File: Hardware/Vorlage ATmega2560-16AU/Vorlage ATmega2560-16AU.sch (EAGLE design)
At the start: 152 parts, among them IC1 CD74HC14PW, IC2 ATMEGA2560640V-8AU, IC3 SS39E, IC4 SS39E, IC5 74AC138D, IC6 XC6210B332MR, Q1 16MHz, Q10 PMV27UPER, Q2 32.768kHz, Q3 PMV27UPER, Q4 PMV27UPER, Q5 PMV27UPER, Q6 PMV27UPER, Q7 PMV27UPER, Q8 PMV27UPER, Q9 PMV27UPER, U1 LM35DZ, X1 2510-, X2 +5V, X3 2514-, X4 2510-, X5 2510-

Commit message: LED Helligkeit mit einstellbarem PWM
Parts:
- added C27: 22nF, rcl:C-EUC0805
- added D1, D2: (no value), diode:DIODE-SOD123
- added R39, R40: 470, rcl:R-EU_R0805
- added R41: 50k, pot:TRIM_EU-3223G
- added V21: PMV20EN, transistor-fet-mit-BSS138:BSS138
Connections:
- new net LED_GND: +5V-POWER.C, V10.S, V11.S, V12.S, V13.S, V14.S, V15.S, V16.S, V17.S, V18.S, V19.S, V20.S, V21.D, V5.S, V6.S, V7.S, V8.S, V9.S
- new net N$36: D1.C, D2.A, IC1F.O, V21.G
- new net N$38: D1.A, R39.1
- new net N$41: D2.C, R40.1
- new net N$42: R39.2, R41.A
- new net N$43: R40.2, R41.E
- new net N$44: C27.1, IC1F.I, R41.S
- net GND: now also C27.2, V21.S; no longer +5V-POWER.C, IC1F.I, V10.S, V11.S, V12.S, V13.S, V14.S, V15.S, V16.S, V17.S, V18.S, V19.S, V20.S, V5.S, V6.S, V7.S, V8.S, V9.S
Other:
- note added: "Abblockkondensatoren"
- note added: "LED Helligkeit mit PWM"
- note removed: "freie Schmitt-Trigger von LCD-Tasten"
- moved on the sheet: IC1F

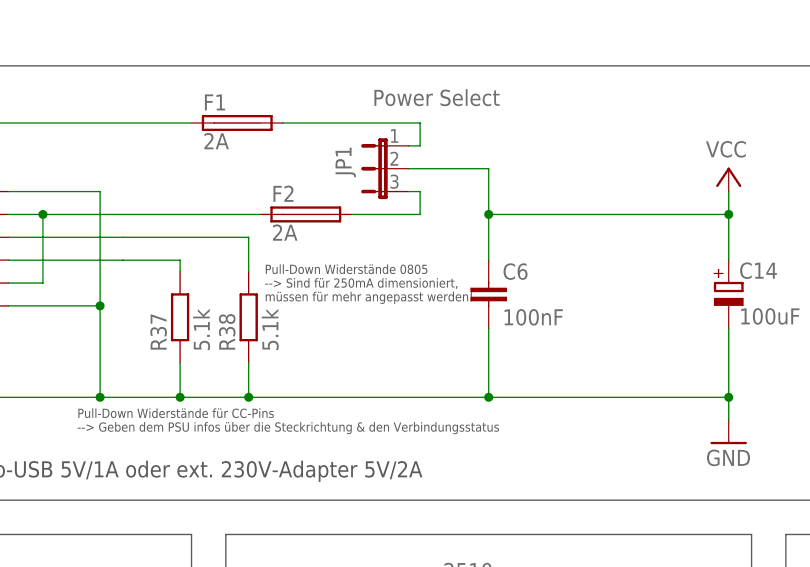
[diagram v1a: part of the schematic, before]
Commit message: 5.1kR Widerstände in BOM und Kommentar in Schema gelöscht
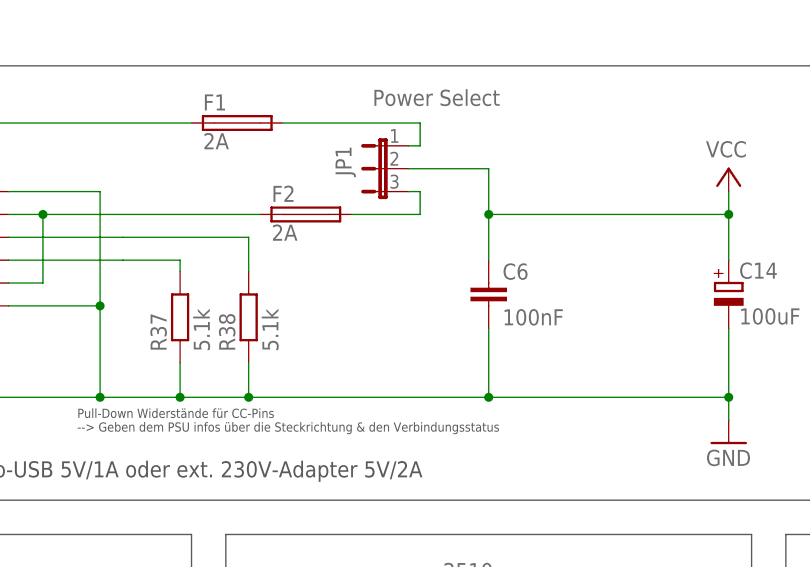
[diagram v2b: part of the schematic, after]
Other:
- note removed: "Pull-Down Widerstände 0805 --> Sind für 250mA dimensioniert, müssen für mehr angepasst werden!"
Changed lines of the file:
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@@
 <text x="53.34" y="-184.15" size="1.016" layer="97">Pull-Down Widerstände für CC-Pins
 --&gt; Geben dem PSU infos über die Steckrichtung &amp; den Verbindungsstatus</text>
-<text x="74.168" y="-169.672" size="1.016" layer="97">Pull-Down Widerstände 0805
---&gt; Sind für 250mA dimensioniert,
-müssen für mehr angepasst werden!</text>
 <wire x1="5.08" y1="66.04" x2="191.77" y2="66.04" width="0.1524" layer="97"/>
 <wire x1="191.77" y1="66.04" x2="191.77" y2="123.19" width="0.1524" layer="97"/>

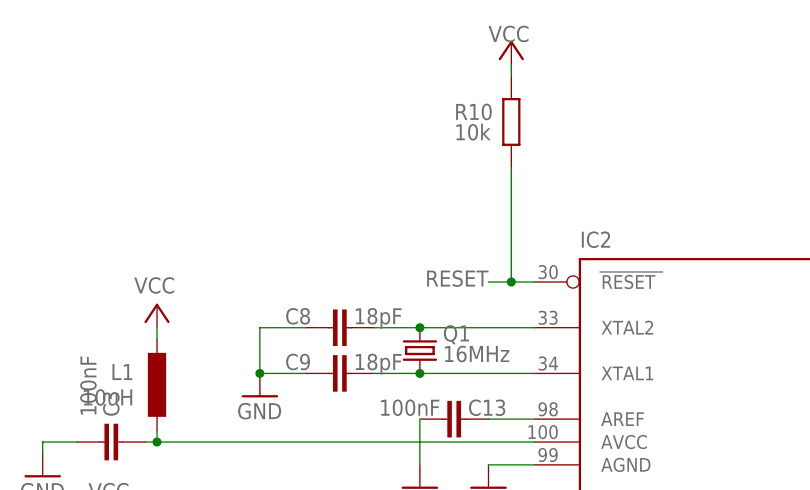
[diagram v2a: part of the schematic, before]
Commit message: Reset button hinzugefügt
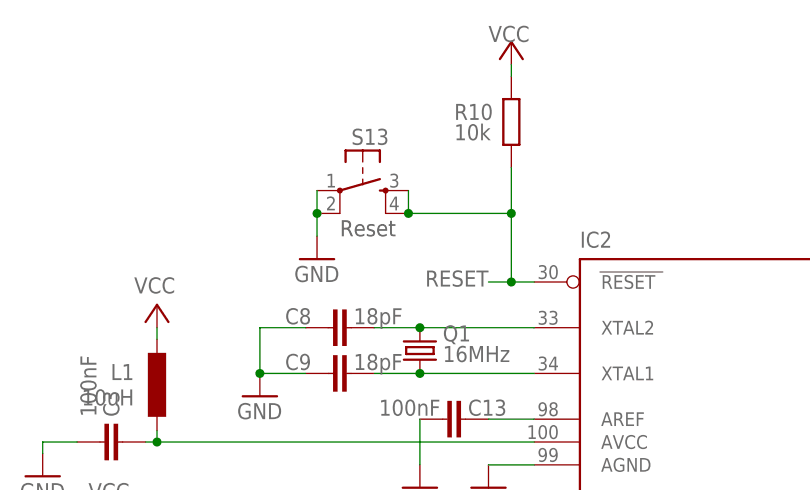
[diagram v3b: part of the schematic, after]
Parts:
- added S13: TS42_4PAD, SmartPrj:TS42_4PAD
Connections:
- net GND: now also S13.1, S13.2
- net RESET: now also S13.3, S13.4
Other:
- note added: "Reset"
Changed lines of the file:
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@@
 <part name="GND32" library="supply1" library_urn="urn:adsk.eagle:library:371" deviceset="GND" device=""/>
 <part name="GND37" library="supply1" library_urn="urn:adsk.eagle:library:371" deviceset="GND" device=""/>
+<part name="S13" library="SmartPrj" deviceset="TS42_4PAD" device="" value=""/>
+<part name="GND39" library="supply1" library_urn="urn:adsk.eagle:library:371" deviceset="GND" device=""/>
 </parts>
 <sheets>
@@
 <wire x1="361.95" y1="-222.25" x2="278.13" y2="-222.25" width="0.1524" layer="97"/>
 <text x="290.83" y="-269.24" size="1.778" layer="97">LED Helligkeit mit PWM</text>
+<text x="110.49" y="330.2" size="1.778" layer="97">Reset</text>
 </plain>
 <instances>
@@
 <instance part="GND37" gate="1" x="342.9" y="-259.08" smashed="yes">
 <attribute name="VALUE" x="340.36" y="-261.62" size="1.778" layer="96"/>
+</instance>
+<instance part="S13" gate="G$1" x="113.03" y="335.28" smashed="yes" rot="R270">
+<attribute name="NAME" x="111.76" y="340.36" size="1.778" layer="95"/>
+</instance>
+<instance part="GND39" gate="1" x="107.95" y="327.66" smashed="yes">
+<attribute name="VALUE" x="105.41" y="325.12" size="1.778" layer="96"/>
 </instance>
 </instances>
@@
 <pinref part="GND37" gate="1" pin="GND"/>
 <wire x1="342.9" y1="-248.92" x2="342.9" y2="-256.54" width="0.1524" layer="91"/>
+</segment>
+<segment>
+<pinref part="S13" gate="G$1" pin="2"/>
+<pinref part="S13" gate="G$1" pin="1"/>
+<wire x1="107.95" y1="332.74" x2="107.95" y2="335.28" width="0.1524" layer="91"/>
+<pinref part="GND39" gate="1" pin="GND"/>
+<wire x1="107.95" y1="332.74" x2="107.95" y2="330.2" width="0.1524" layer="91"/>
+<junction x="107.95" y="332.74"/>
 </segment>
 </net>
@@
 <pinref part="IC2" gate="1" pin="RESET"/>
 <wire x1="132.08" y1="325.12" x2="129.54" y2="325.12" width="0.1524" layer="91"/>
-<wire x1="129.54" y1="325.12" x2="129.54" y2="337.82" width="0.1524" layer="91"/>
+<wire x1="129.54" y1="325.12" x2="129.54" y2="332.74" width="0.1524" layer="91"/>
+<wire x1="129.54" y1="332.74" x2="129.54" y2="337.82" width="0.1524" layer="91"/>
 <wire x1="129.54" y1="325.12" x2="127" y2="325.12" width="0.1524" layer="91"/>
 <junction x="129.54" y="325.12"/>
 <label x="127" y="326.39" size="1.778" layer="95" rot="R180"/>
-</segment>
-<segment>
+<pinref part="S13" gate="G$1" pin="3"/>
+<pinref part="S13" gate="G$1" pin="4"/>
+<wire x1="118.11" y1="335.28" x2="118.11" y2="332.74" width="0.1524" layer="91"/>
+<wire x1="118.11" y1="332.74" x2="129.54" y2="332.74" width="0.1524" layer="91"/>
+<junction x="118.11" y="332.74"/>
+<junction x="129.54" y="332.74"/>
+</segment>
+<segment>
